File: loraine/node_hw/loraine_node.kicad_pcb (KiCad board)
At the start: 2 copper layers, 27 parts, among them CON1 BARREL_JACK, IC1 ATTINY2313A-S, P1 MOLEX, P2 MOLEX, P4 ICSP, P5 OUTPUTS, P6 BUS, Q1 FZT600, Q2 FZT600, Q3 FZT600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

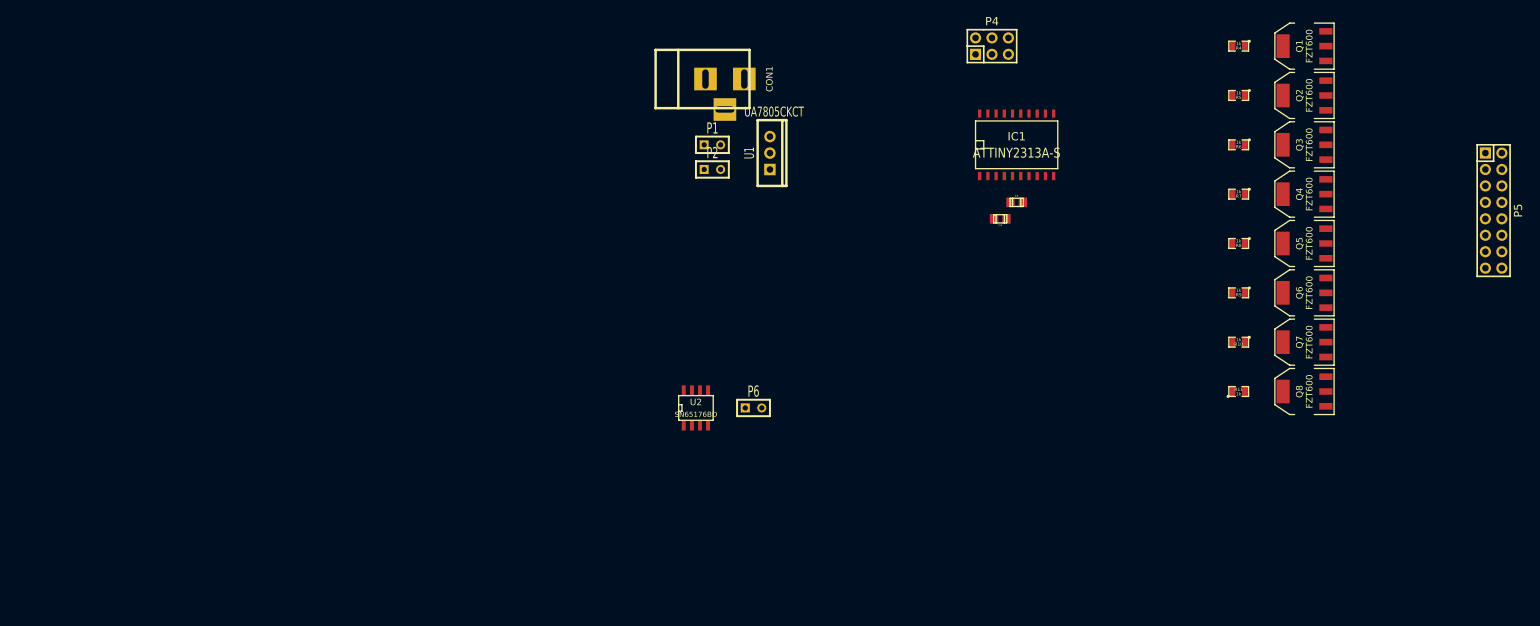
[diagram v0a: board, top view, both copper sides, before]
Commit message: First attempt at PCB, minus some caps and LEDs
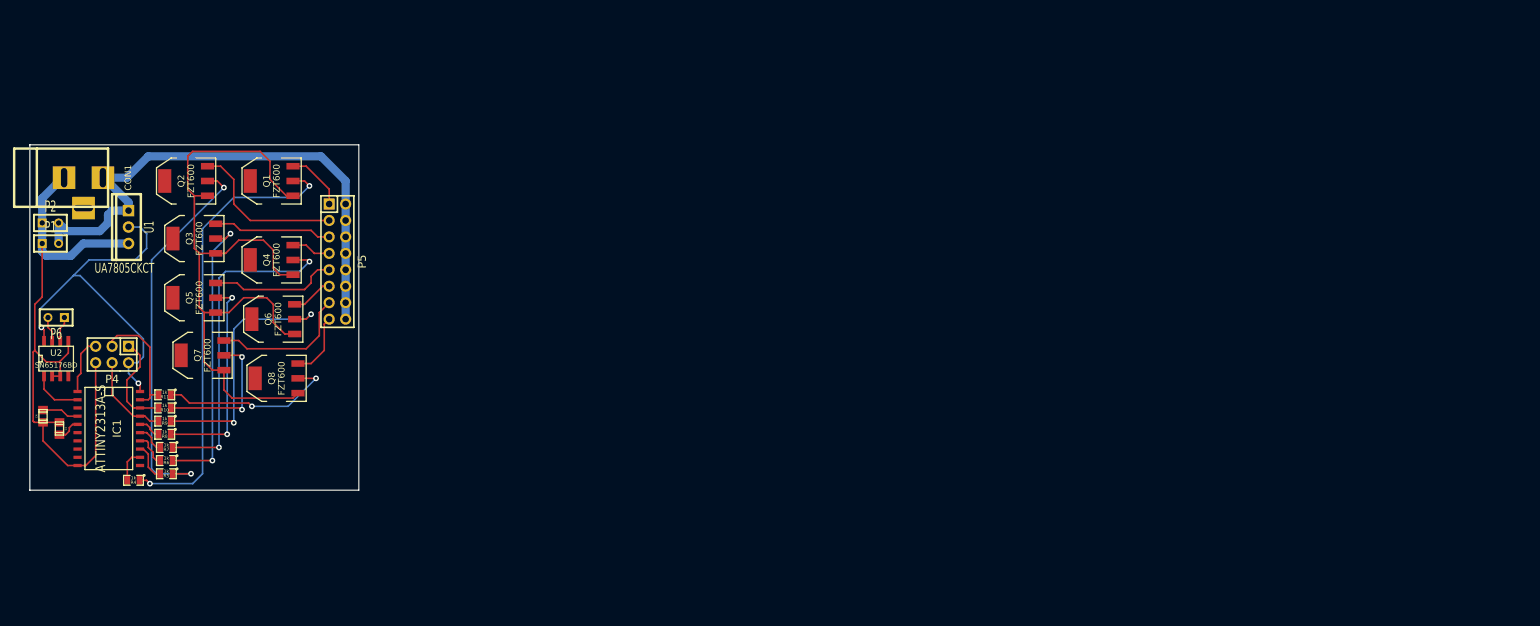
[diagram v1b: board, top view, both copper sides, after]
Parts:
- moved R4 183.4 mm to (66.8, 102.6)
- moved P5 178.7 mm to (98.3, 68.8)
- moved R5 175.6 mm to (71.9, 101.6)
- moved Q2 173.2 mm to (74.9, 56.4)
- moved R6 172.6 mm to (71.9, 99.6)
- moved Q3 172.1 mm to (76.2, 65.3)
- moved Q5 171.7 mm to (76.2, 74.4)
- moved Q7 170.2 mm to (77.5, 83.3)
- moved R7 170.2 mm to (71.9, 97.5)
- moved R8 168.5 mm to (71.6, 95.5)
- moved R9 167.0 mm to (71.6, 93.5)
- moved R10 166.2 mm to (71.6, 91.4)
- moved R11 165.9 mm to (71.6, 89.4), turned to 180 degrees
- moved Q1 160.9 mm to (88.1, 56.4)
- moved Q4 159.8 mm to (88.1, 68.6)
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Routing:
- net GND: track 0.00 -> 211.7 mm
- net +12V: track 0.00 -> 85.1 mm
- net Net-(Q1-Pad2): track 0.00 -> 70.5 mm, vias 0 -> 2
- net Net-(Q2-Pad2): track 0.00 -> 60.3 mm, vias 0 -> 2
- net VCC: track 0.00 -> 56.6 mm, vias 0 -> 2
- net Net-(Q4-Pad2): track 0.00 -> 51.0 mm, vias 0 -> 2
- net Net-(Q3-Pad2): track 0.00 -> 45.0 mm, vias 0 -> 2
- net Net-(Q6-Pad2): track 0.00 -> 40.0 mm, vias 0 -> 2
- net Net-(Q5-Pad2): track 0.00 -> 32.6 mm, vias 0 -> 2
- net Net-(Q8-Pad2): track 0.00 -> 27.7 mm, vias 0 -> 2
- net Net-(D2-Pad2): track 0.00 -> 24.5 mm
- net Net-(Q7-Pad2): track 0.00 -> 22.1 mm, vias 0 -> 2
- net Net-(P5-Pad13): track 0.00 -> 21.8 mm
- net Net-(P5-Pad9): track 0.00 -> 19.8 mm
- net /SCK: track 0.00 -> 18.6 mm
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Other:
- board outline added: 50.8 x 53.3 mm
- net class chunky added: clearance 0.254, trace_width 1.27, via_dia 0.889, via_drill 0.635
- net class signal added: clearance 0.254, trace_width 0.254, via_dia 0.889, via_drill 0.635

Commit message: Changed darlingtons to PTH part
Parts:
- Q1, Q2, Q3, Q4, Q5, Q6, Q7, Q8: value FZT600 -> BD679; footprint SMD_Packages:SOT223 -> to126:TO126
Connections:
- Q1 pad 2: Net-(Q1-Pad2) -> Net-(D1-Pad2)
- Q1 pad 3: Net-(D1-Pad2) -> Net-(Q1-Pad3)
- Q2 pad 2: Net-(Q2-Pad2) -> Net-(D2-Pad2)
- Q2 pad 3: Net-(D2-Pad2) -> Net-(Q2-Pad3)
- Q3 pad 2: Net-(Q3-Pad2) -> Net-(D3-Pad2)
- Q3 pad 3: Net-(D3-Pad2) -> Net-(Q3-Pad3)
- Q4 pad 2: Net-(Q4-Pad2) -> Net-(P5-Pad7)
- Q4 pad 3: Net-(P5-Pad7) -> Net-(Q4-Pad3)
- Q5 pad 2: Net-(Q5-Pad2) -> Net-(P5-Pad9)
- Q5 pad 3: Net-(P5-Pad9) -> Net-(Q5-Pad3)
- Q6 pad 2: Net-(Q6-Pad2) -> Net-(P5-Pad11)
- Q6 pad 3: Net-(P5-Pad11) -> Net-(Q6-Pad3)
- Q7 pad 2: Net-(Q7-Pad2) -> Net-(P5-Pad13)
- Q7 pad 3: Net-(P5-Pad13) -> Net-(Q7-Pad3)
- Q8 pad 2: Net-(Q8-Pad2) -> Net-(P5-Pad15)
- Q8 pad 3: Net-(P5-Pad15) -> Net-(Q8-Pad3)
- R10 pad 1: Net-(Q7-Pad2) -> Net-(Q7-Pad3)
- R11 pad 1: Net-(Q8-Pad2) -> Net-(Q8-Pad3)
- R4 pad 1: Net-(Q1-Pad2) -> Net-(Q1-Pad3)
- R5 pad 1: Net-(Q2-Pad2) -> Net-(Q2-Pad3)
- R6 pad 1: Net-(Q3-Pad2) -> Net-(Q3-Pad3)
- R7 pad 1: Net-(Q4-Pad2) -> Net-(Q4-Pad3)
- R8 pad 1: Net-(Q5-Pad2) -> Net-(Q5-Pad3)
- R9 pad 1: Net-(Q6-Pad2) -> Net-(Q6-Pad3)
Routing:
- net Net-(Q6-Pad3): track 0.00 -> 132.9 mm, vias 0 -> 2
- net GND: track 211.7 -> 98.9 mm
- net Net-(Q1-Pad3): track 0.00 -> 90.5 mm, vias 0 -> 2
- net Net-(Q1-Pad2): track 70.5 -> 0.00 mm, vias 2 -> 0
- net Net-(Q2-Pad3): track 0.00 -> 60.3 mm, vias 0 -> 2
- net Net-(Q2-Pad2): track 60.3 -> 0.00 mm, vias 2 -> 0
- net Net-(Q4-Pad3): track 0.00 -> 51.0 mm, vias 0 -> 2
- net Net-(Q4-Pad2): track 51.0 -> 0.00 mm, vias 2 -> 0
- net Net-(Q3-Pad3): track 0.00 -> 45.0 mm, vias 0 -> 2
- net Net-(Q3-Pad2): track 45.0 -> 0.00 mm, vias 2 -> 0
- net Net-(Q6-Pad2): track 40.0 -> 0.00 mm, vias 2 -> 0
- net Net-(Q5-Pad3): track 0.00 -> 32.6 mm, vias 0 -> 2
- net Net-(Q5-Pad2): track 32.6 -> 0.00 mm, vias 2 -> 0
- net Net-(Q8-Pad3): track 0.00 -> 27.7 mm, vias 0 -> 2
- net Net-(Q8-Pad2): track 27.7 -> 0.00 mm, vias 2 -> 0
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
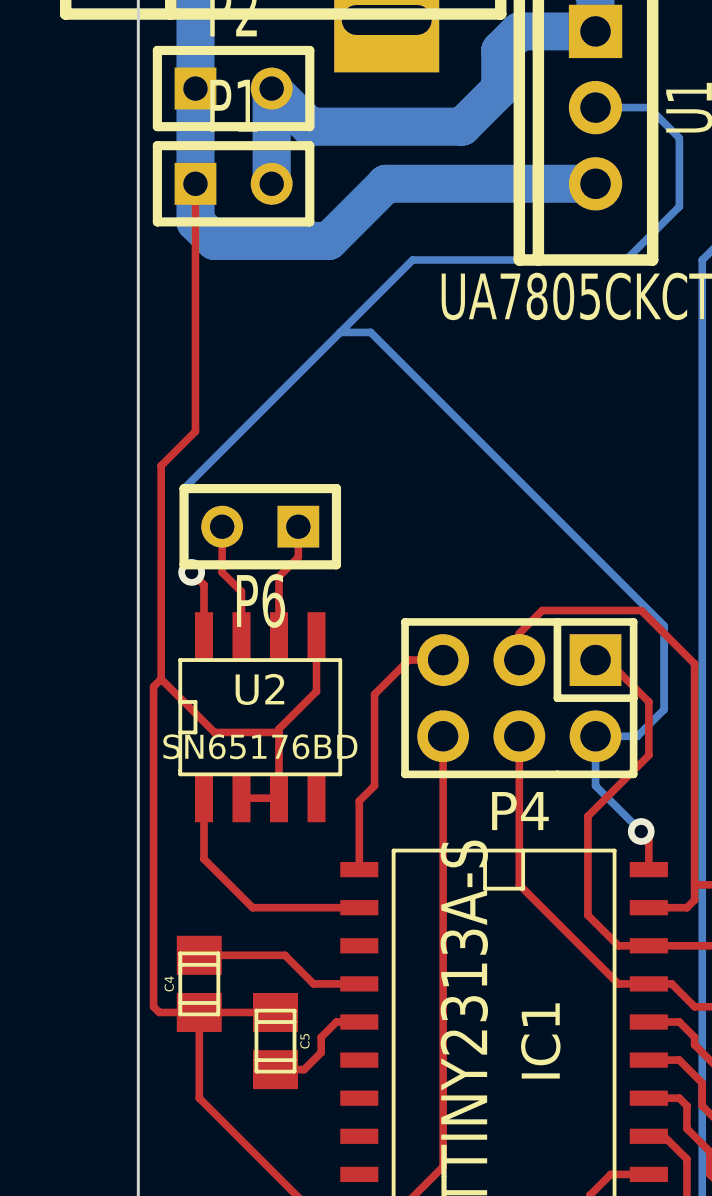
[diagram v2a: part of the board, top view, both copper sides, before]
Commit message: Added bus thu connector
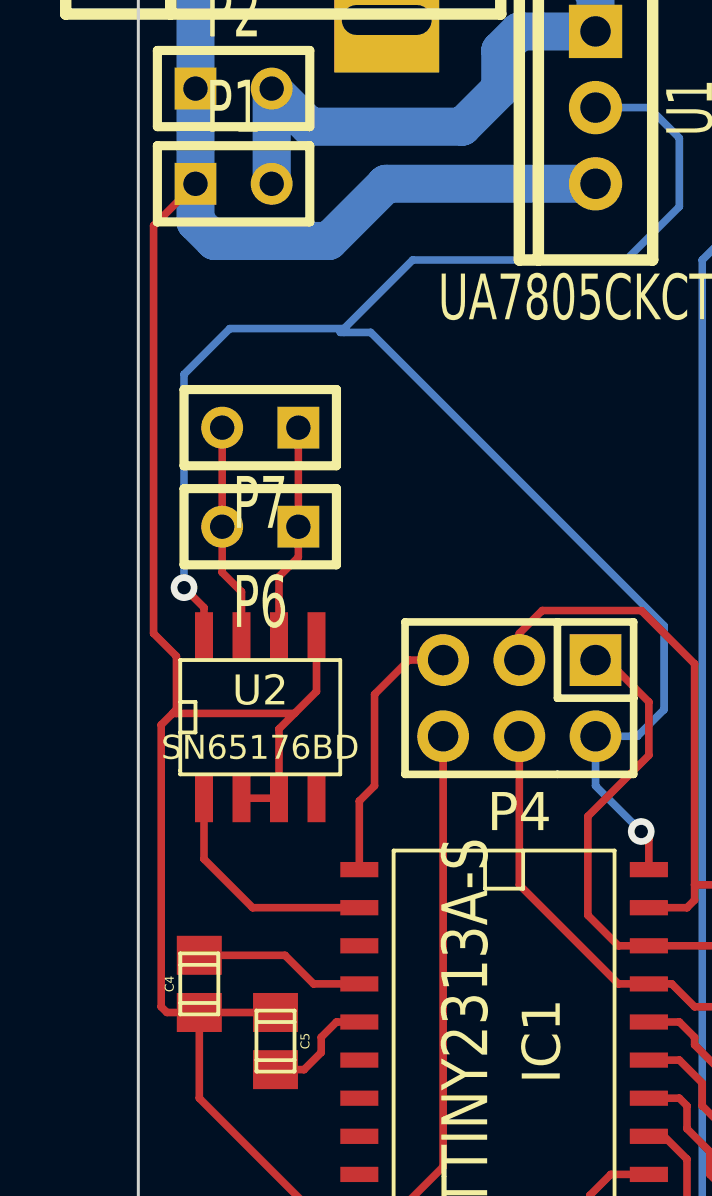
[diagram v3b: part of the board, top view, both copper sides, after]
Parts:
- added P7: BUS_THRU, Connect:SIL-2, F.Cu at (54.9, 74.2)
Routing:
- net Net-(Q6-Pad3): track 132.9 -> 51.9 mm
- net Net-(Q1-Pad3): track 90.5 -> 171.5 mm
- net Net-(P6-Pad1): track 3.92 -> 7.22 mm
- net Net-(P6-Pad2): track 3.92 -> 7.22 mm
- net VCC: track 56.6 -> 59.1 mm

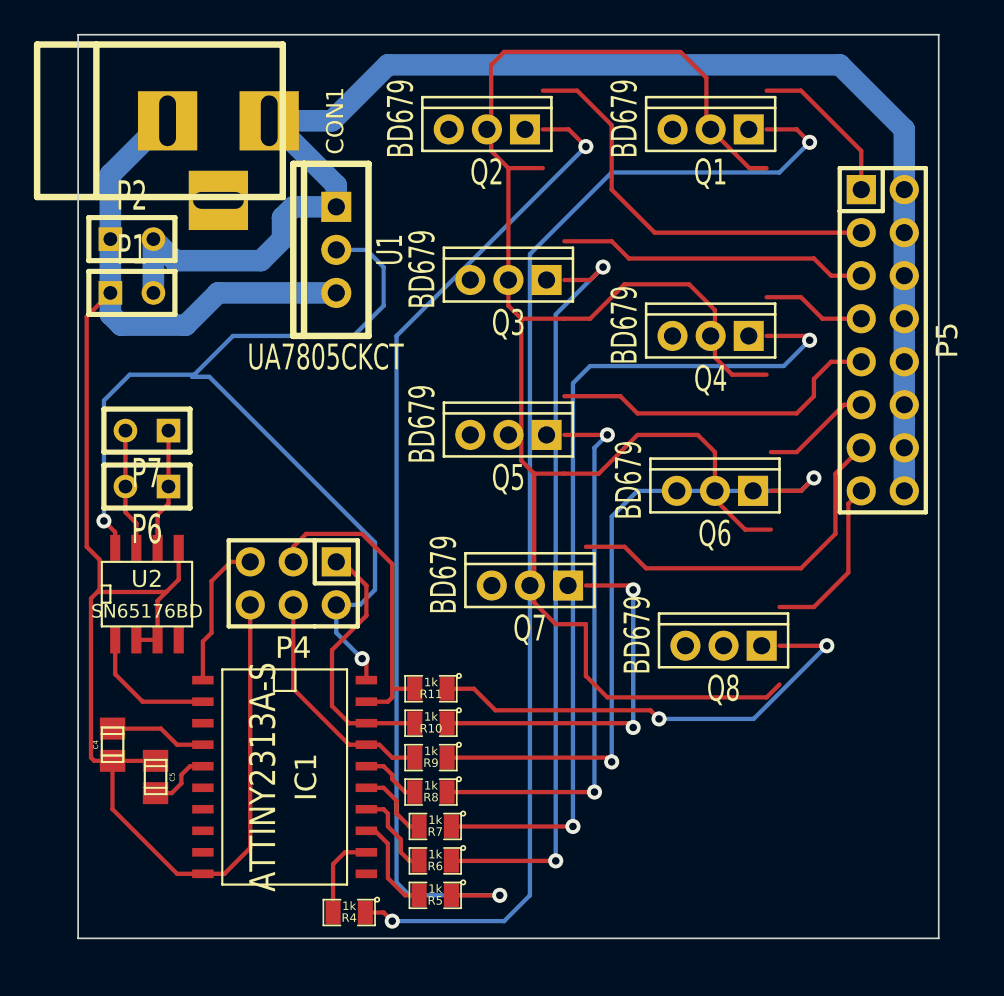
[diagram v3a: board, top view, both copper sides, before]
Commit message: PCB rev2
Routed PTH darlingtons
swapped order of output pinout to make pcb route better
'L'-shaped PCB for adam ;)
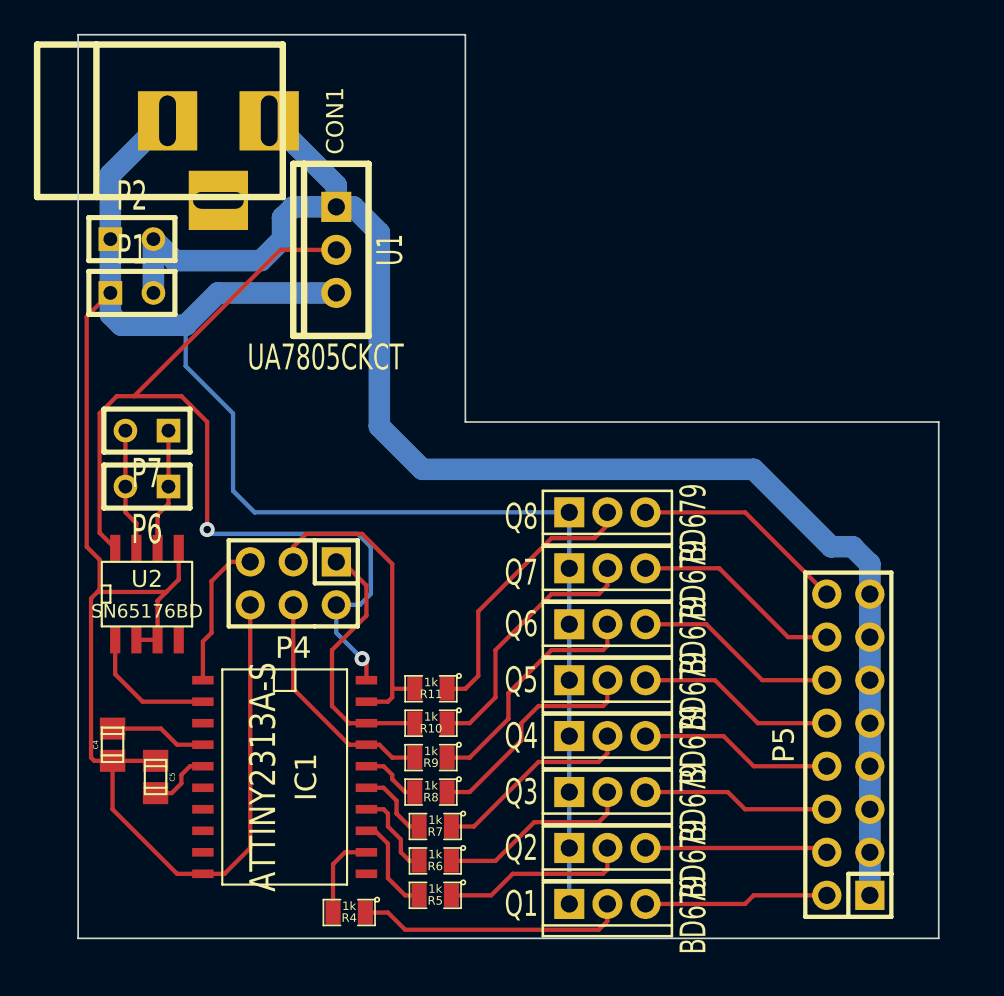
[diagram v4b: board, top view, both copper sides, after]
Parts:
- moved Q1 46.1 mm to (82.0, 102.1), turned to 270 degrees
- moved Q2 43.0 mm to (82.0, 98.8), turned to 270 degrees
- moved Q3 30.8 mm to (82.0, 95.5), turned to 270 degrees
- moved Q4 24.4 mm to (82.0, 92.2), turned to 270 degrees
- moved P5 24.0 mm to (96.3, 92.7), turned to 90 degrees
- moved Q5 15.6 mm to (82.0, 88.9), turned to 270 degrees
- moved Q8 10.4 mm to (82.0, 79.0), turned to 270 degrees
- moved Q6 10.1 mm to (82.0, 85.6), turned to 270 degrees
- moved Q7 4.68 mm to (82.0, 82.3), turned to 270 degrees
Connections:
- P5 pad 1: Net-(D1-Pad2) -> +12V
- P5 pad 10: +12V -> Net-(P5-Pad10)
- P5 pad 11: Net-(P5-Pad11) -> +12V
- P5 pad 12: +12V -> Net-(P5-Pad12)
- P5 pad 13: Net-(P5-Pad13) -> +12V
- P5 pad 14: +12V -> Net-(P5-Pad14)
- P5 pad 15: Net-(P5-Pad15) -> +12V
- P5 pad 16: +12V -> Net-(P5-Pad16)
- P5 pad 2: +12V -> Net-(D1-Pad2)
- P5 pad 3: Net-(D2-Pad2) -> +12V
- P5 pad 4: +12V -> Net-(D2-Pad2)
- P5 pad 5: Net-(D3-Pad2) -> +12V
- P5 pad 6: +12V -> Net-(D3-Pad2)
- P5 pad 7: Net-(P5-Pad7) -> +12V
- P5 pad 8: +12V -> Net-(P5-Pad8)
- P5 pad 9: Net-(P5-Pad9) -> +12V
- Q4 pad 2: Net-(P5-Pad7) -> Net-(P5-Pad8)
- Q5 pad 2: Net-(P5-Pad9) -> Net-(P5-Pad10)
- Q6 pad 2: Net-(P5-Pad11) -> Net-(P5-Pad12)
- Q7 pad 2: Net-(P5-Pad13) -> Net-(P5-Pad14)
- Q8 pad 2: Net-(P5-Pad15) -> Net-(P5-Pad16)
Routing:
- net Net-(Q1-Pad3): track 171.5 -> 15.9 mm, vias 2 -> 0
- net GND: track 98.8 -> 153.3 mm
- net Net-(Q2-Pad3): track 60.3 -> 11.1 mm, vias 2 -> 0
- net Net-(Q4-Pad3): track 51.0 -> 12.0 mm, vias 2 -> 0
- net Net-(Q6-Pad3): track 51.9 -> 14.4 mm, vias 2 -> 0
- net Net-(Q3-Pad3): track 45.0 -> 11.6 mm, vias 2 -> 0
- net Net-(P5-Pad13): track 21.8 -> 0.00 mm
- net Net-(P5-Pad9): track 19.8 -> 0.00 mm
- net Net-(Q5-Pad3): track 32.6 -> 13.5 mm, vias 2 -> 0
- net Net-(D2-Pad2): track 24.5 -> 10.8 mm
- net Net-(P5-Pad16): track 0.00 -> 12.7 mm
- net Net-(P5-Pad14): track 0.00 -> 12.4 mm
- net Net-(P5-Pad12): track 0.00 -> 12.1 mm
- net Net-(P5-Pad10): track 0.00 -> 11.8 mm
- net Net-(P5-Pad8): track 0.00 -> 11.4 mm
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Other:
- outline, holes or cut-outs redrawn

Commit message: Added TL4242 footprint
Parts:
- added U3: TL4242, 8-son:8-SON, F.Cu at (66.0, 111.8)
- added U4: TL4242, 8-son:8-SON, F.Cu at (85.1, 114.3)
- added U5: TL4242, 8-son:8-SON, F.Cu at (76.2, 111.8)

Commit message: Added star led module footprint
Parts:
- added D1: STAR_LED, led_module:led_module, F.Cu at (86.6, 65.4)
- moved U4 60.7 mm to (85.2, 53.6)
- moved U5 59.8 mm to (93.9, 54.6)
- moved U3 58.3 mm to (76.5, 54.4)

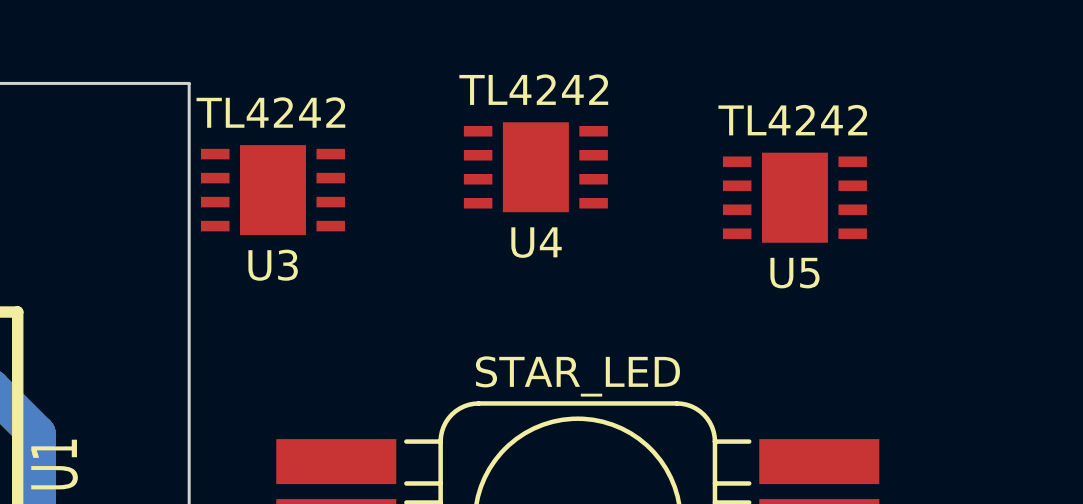
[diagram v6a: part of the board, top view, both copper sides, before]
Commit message: Added outline to 8-SON footprint
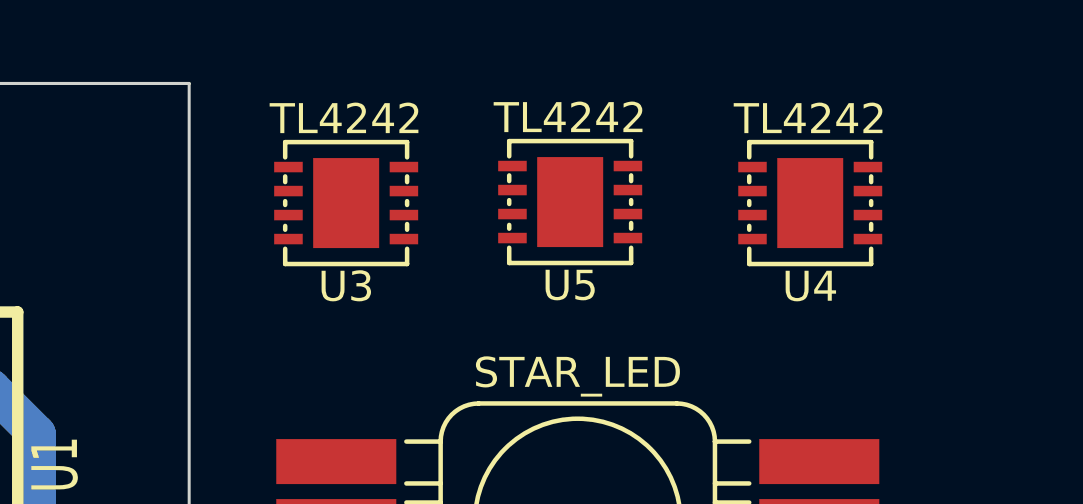
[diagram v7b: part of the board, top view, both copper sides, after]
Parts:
- moved U4 9.22 mm to (94.4, 54.8)
- moved U5 7.49 mm to (86.4, 54.8)
- moved U3 2.48 mm to (78.9, 54.8)
